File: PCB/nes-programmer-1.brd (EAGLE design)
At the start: 130 x 50 mm, 32 parts, among them J3 Molex 22-28-8062, M1 ATmega328P Module, M2 0124A, SW1 Push Switch, U1 MCP23S08, U2 MCP23S17

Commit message: Final tweaks.
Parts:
- removed J3: Molex 22-28-8062, con-headers:MA06X1-RA-THD
- removed SW1: Push Switch, switch-smd:B3SN
- added ACT: (no value), led:SMD_0603
- added R18: 2K, rlc:0603-RES
- added RESET: Push Switch, switch-smd:B3SN
- added SERIAL: Molex 22-28-8062, con-headers:MA06X1-RA-THD
- moved ICSP 41.4 mm to (87.0, 5.00), turned to 180 degrees
- moved R1 25.9 mm to (14.0, 30.6)
- moved C3 8.25 mm to (88.8, 13.2)
- moved C4 8.25 mm to (90.8, 13.2)
- moved C5 8.25 mm to (82.8, 13.2)
- moved VR33 8.25 mm to (85.8, 13.2)
- moved R12 5.66 mm to (17.4, 30.6), turned to 90 degrees
- moved R7 5.06 mm to (37.0, 7.20), turned to 270 degrees
- moved R11 4.00 mm to (35.0, 15.2)
- moved R5 3.76 mm to (16.0, 30.6), turned to 270 degrees
- moved R10 3.61 mm to (6.00, 10.4)
- moved R16 3.40 mm to (112.6, 20.2)
- moved R17 3.40 mm to (112.6, 22.8)
- moved R8 3.01 mm to (15.0, 4.10)
- moved R9 3.01 mm to (13.0, 4.10)
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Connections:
- new net ACTIVITY: M1.D6, R18.1
- new net ACT_LED: ACT.A, R18.2
- net !RESET: now also RESET.3, RESET.4; no longer SW1.3, SW1.4
- net FT_RX: now also SERIAL.5; no longer J3.5
- net FT_TX: now also SERIAL.4; no longer J3.4
- net GND: now also ACT.K, RESET.1, RESET.2, SERIAL.1; no longer J3.1, SW1.1, SW1.2
- net SD_!DET: now also M1.D7; no longer M1.D6
- net VCC: now also SERIAL.3; no longer J3.3
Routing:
- net VCC: track 0.00 -> 221.8 mm, vias 0 -> 5
- net SPI_MOSI: track 0.00 -> 134.9 mm, vias 0 -> 5
- net SPI_SCK: track 0.00 -> 133.7 mm, vias 0 -> 5
- net SPI_MISO: track 0.00 -> 130.0 mm, vias 0 -> 5
- net TX: track 0.00 -> 111.9 mm, vias 0 -> 2
- net RX: track 0.00 -> 109.6 mm, vias 0 -> 2
- net ADDR_!CS: track 0.00 -> 106.5 mm, vias 0 -> 2
- net !RESET: track 0.00 -> 100.6 mm, vias 0 -> 4
- net +3.3V: track 0.00 -> 88.3 mm, vias 0 -> 3
- net SD_!DET: track 0.00 -> 65.8 mm, vias 0 -> 2
- net PGM_!OE: track 0.00 -> 60.4 mm, vias 0 -> 2
- net PGM_!WR: track 0.00 -> 59.6 mm, vias 0 -> 2
- net ACT_LED: track 0.00 -> 54.2 mm, vias 0 -> 2
- net CHR_!WR: track 0.00 -> 50.1 mm, vias 0 -> 2
- net CIC_+RST: track 0.00 -> 47.0 mm, vias 0 -> 1
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- added copper zone on layer 1, net GND
- added copper zone on layer 16, net GND
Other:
- board size 130 x 50 mm -> 126 x 48 mm
- board text added: "M n e m o s y n e"
- board text added: "MNEMOSYNE"
- board text added: "NES Programmer"
- board text added: "RX"
- board text added: "Rev. A (2023-12)"
- board text added: "TX"
- board text added: "by Circuit Monkey"

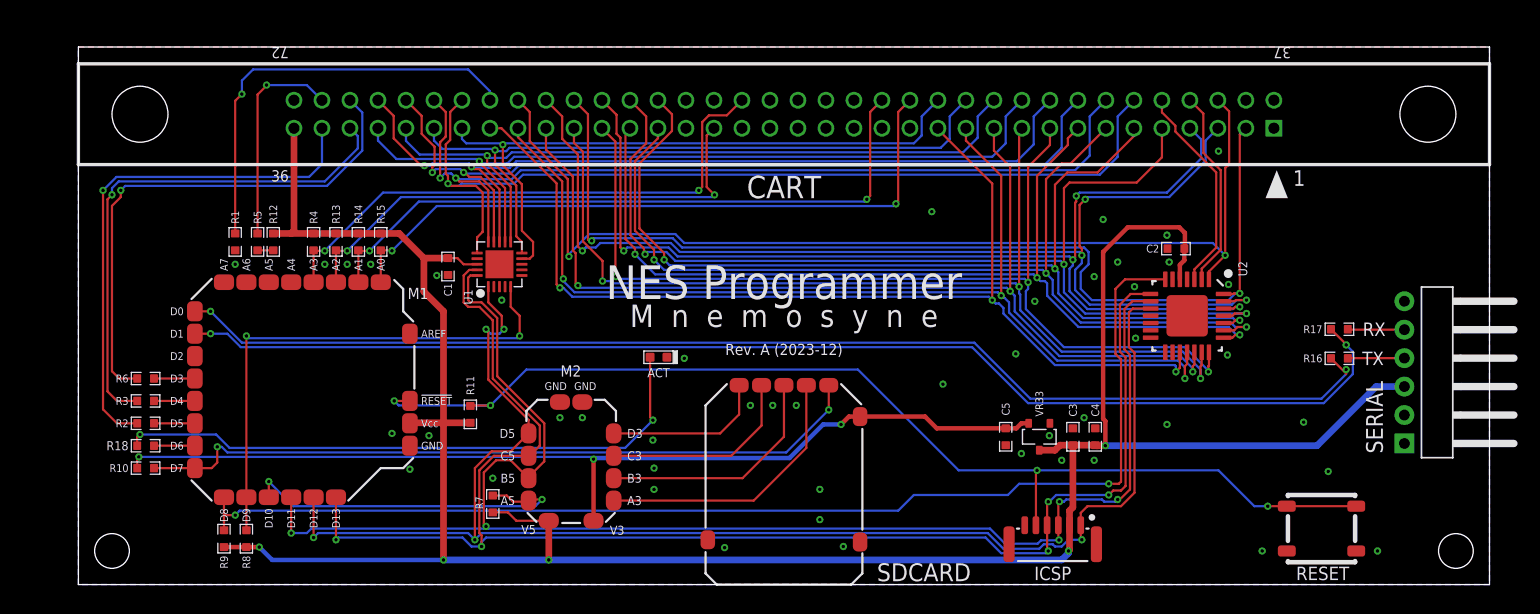
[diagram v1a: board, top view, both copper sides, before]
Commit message: Bump rev to B. Fix connector hole spacing issue.
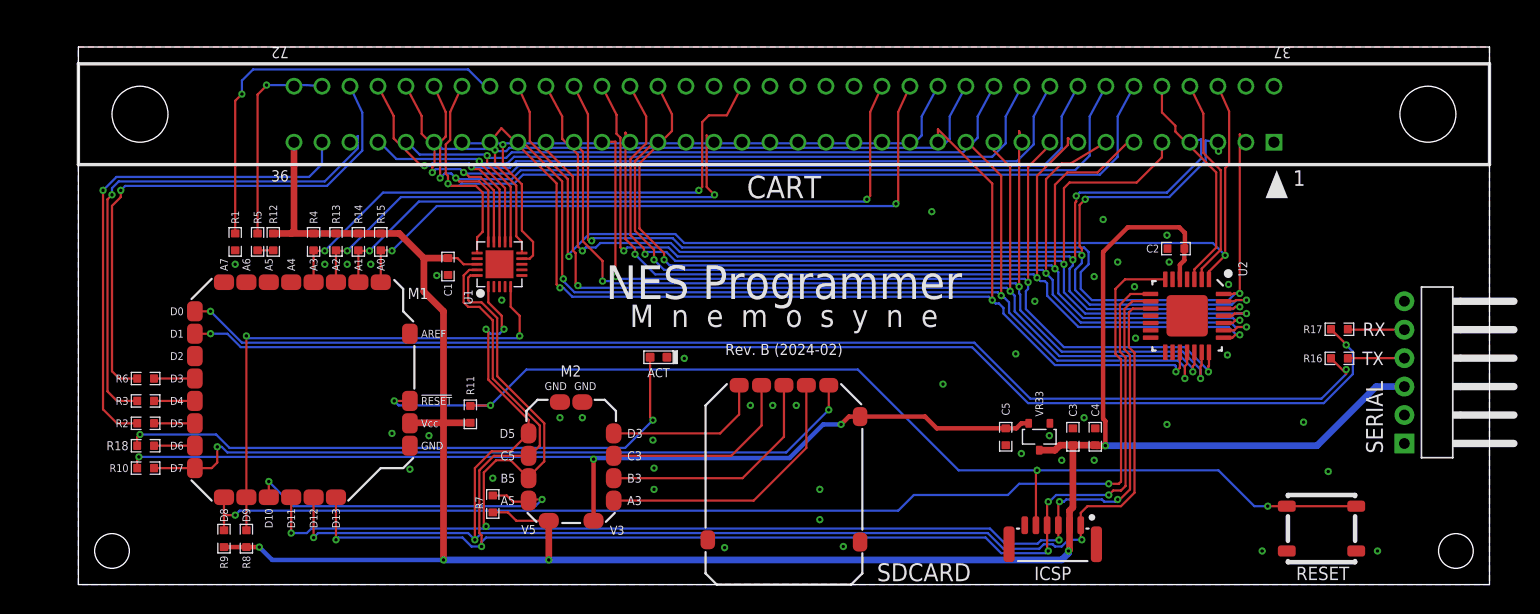
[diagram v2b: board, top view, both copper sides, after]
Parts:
- C1, C2, C3: value (none) -> 0.1uF
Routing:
- net A2: track 91.3 -> 88.8 mm
- net A12: track 93.3 -> 95.4 mm
- net D7: track 83.8 -> 85.8 mm
- net D6: track 80.3 -> 82.4 mm
- net D5: track 77.8 -> 79.9 mm
- net D4: track 75.9 -> 77.9 mm
- net A4: track 88.3 -> 86.5 mm
- net A0: track 95.4 -> 97.0 mm
- net A6: track 87.3 -> 85.9 mm
- net A1: track 94.2 -> 92.9 mm
- net VCC: track 221.8 -> 220.6 mm
- net CIC_2MB: track 46.8 -> 45.6 mm
- net A14: track 18.8 -> 20.1 mm
- net A11: track 93.3 -> 94.4 mm
- net PGM_!WR: track 59.6 -> 60.6 mm
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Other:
- board text added: "Rev. B (2024-02)"
- board text removed: "Rev. A (2023-12)"
